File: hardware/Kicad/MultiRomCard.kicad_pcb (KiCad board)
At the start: 2 copper layers, 160 x 100 mm, 16 parts, among them P1 VC4000_Cartridge_Bus, U1 Arduino_UNO, U2 74HC595, U3 74HC595, U4 74HC595, U5 6264, U6 74HC245, U7 74HC245, U8 74HC245

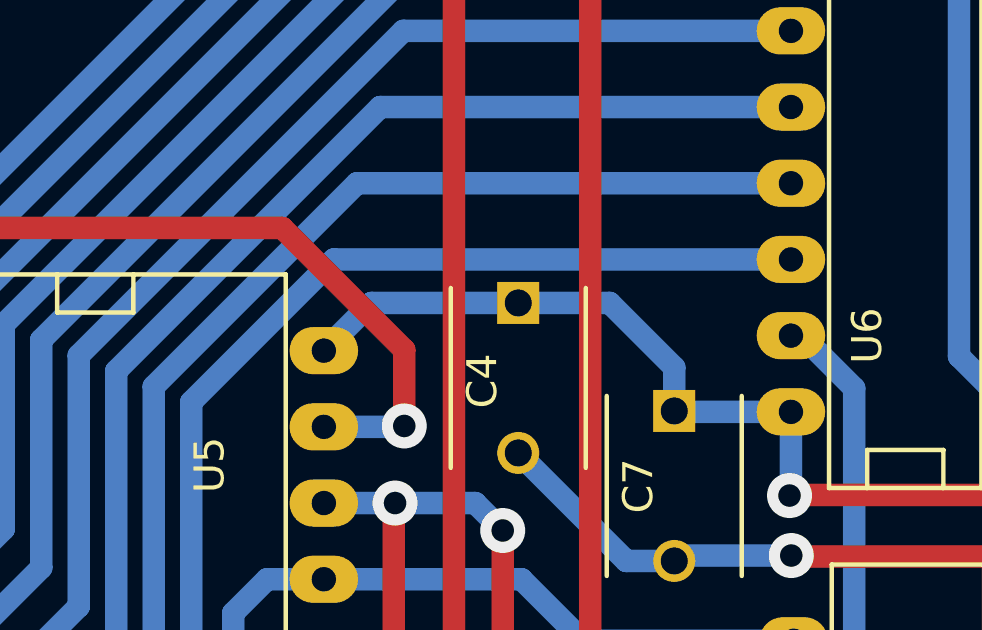
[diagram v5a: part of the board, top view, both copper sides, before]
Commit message: [PCB] Corrected DRC error (track near pad).
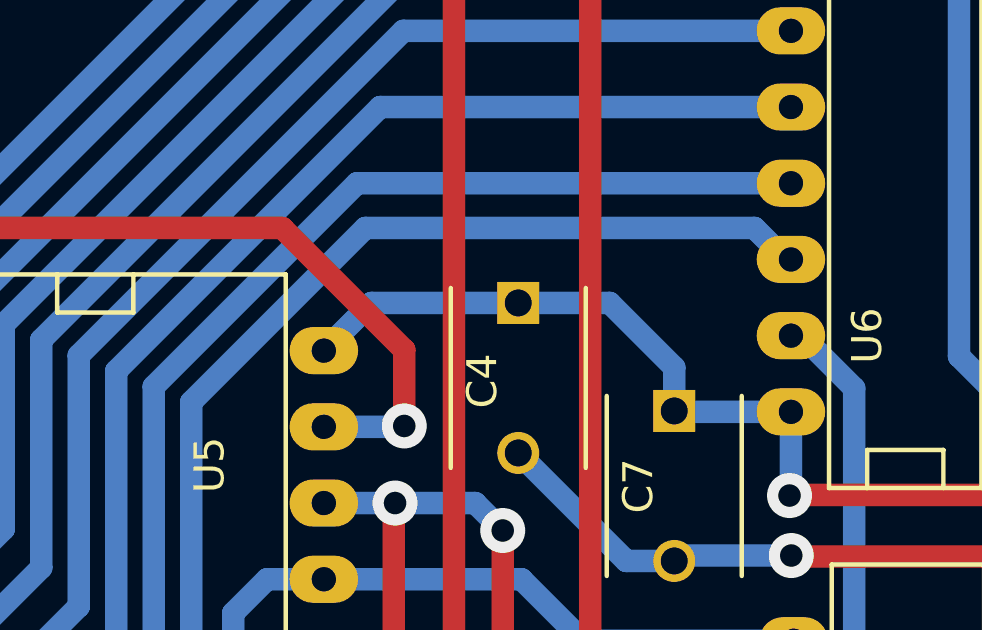
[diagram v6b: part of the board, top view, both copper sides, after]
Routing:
- net /A0: track 105.2 -> 106.1 mm
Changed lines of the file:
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@@
     (thickness 1.6)
     (drawings 8)
-    (tracks 851)
+    (tracks 853)
     (zones 0)
     (modules 16)
@@
   (segment (start 150.91196 90.99756) (end 150.91196 87.723648) (width 0.75) (layer B.Cu) (net 11))
   (segment (start 156.3244 96.41) (end 150.91196 90.99756) (width 0.75) (layer B.Cu) (net 11) (status 10))
+  (segment (start 156.68 98.95) (end 157.0356 98.95) (width 0.75) (layer B.Cu) (net 12))
+  (segment (start 157.0356 98.95) (end 167.5 88.4856) (width 0.75) (layer B.Cu) (net 12))
+  (segment (start 167.5 88.4856) (end 167.5 77.803398) (width 0.75) (layer B.Cu) (net 12))
+  (segment (start 186.273398 72) (end 187.323398 73.05) (width 0.75) (layer B.Cu) (net 12))
+  (segment (start 167.5 77.803398) (end 173.303398 72) (width 0.75) (layer B.Cu) (net 12))
+  (segment (start 173.303398 72) (end 186.273398 72) (width 0.75) (layer B.Cu) (net 12))
+  (segment (start 187.323398 73.05) (end 187.49 73.05) (width 0.75) (layer B.Cu) (net 12))
   (segment (start 126.1 80.8) (end 126.1 78.8) (width 0.75) (layer B.Cu) (net 12))
   (segment (start 126.1 78.8) (end 127.474999 77.425001) (width 0.75) (layer B.Cu) (net 12))
@@
   (segment (start 156.3244 98.95) (end 149.66195 92.28755) (width 0.75) (layer B.Cu) (net 12))
   (via (at 141.047851 80.627475) (size 1.5) (drill 0.75) (layers F.Cu B.Cu) (net 12))
-  (segment (start 156.68 98.95) (end 157.0356 98.95) (width 0.75) (layer B.Cu) (net 12) (status 30))
-  (segment (start 167.5 88.4856) (end 167.5 77.803398) (width 0.75) (layer B.Cu) (net 12))
-  (segment (start 157.0356 98.95) (end 167.5 88.4856) (width 0.75) (layer B.Cu) (net 12) (status 10))
-  (segment (start 167.5 77.803398) (end 172.253398 73.05) (width 0.75) (layer B.Cu) (net 12))
-  (segment (start 172.253398 73.05) (end 187.49 73.05) (width 0.75) (layer B.Cu) (net 12) (status 20))
   (via (at 126.1 80.8) (size 1.5) (drill 0.75) (layers F.Cu B.Cu) (net 12))
   (segment (start 197.231869 111.275116) (end 197.231869 106.868131) (width 0.75) (layer B.Cu) (net 13))
